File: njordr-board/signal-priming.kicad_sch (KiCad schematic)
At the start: 42 parts, among them IC2 GS8054, IC3 TMUX741x, T1 TestPoint, T10 TestPoint, T11 TestPoint, T2 TestPoint, T9 TestPoint, U3 REF3012, U7 LM393

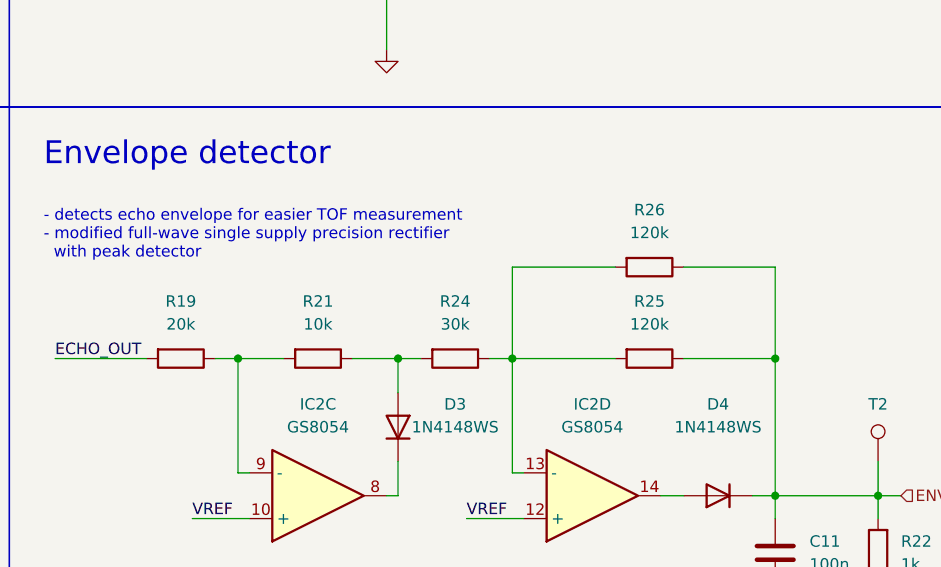
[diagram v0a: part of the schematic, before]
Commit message: board: Use lower resistor values for the envelope detector
- try to lower impedance to have higher stability
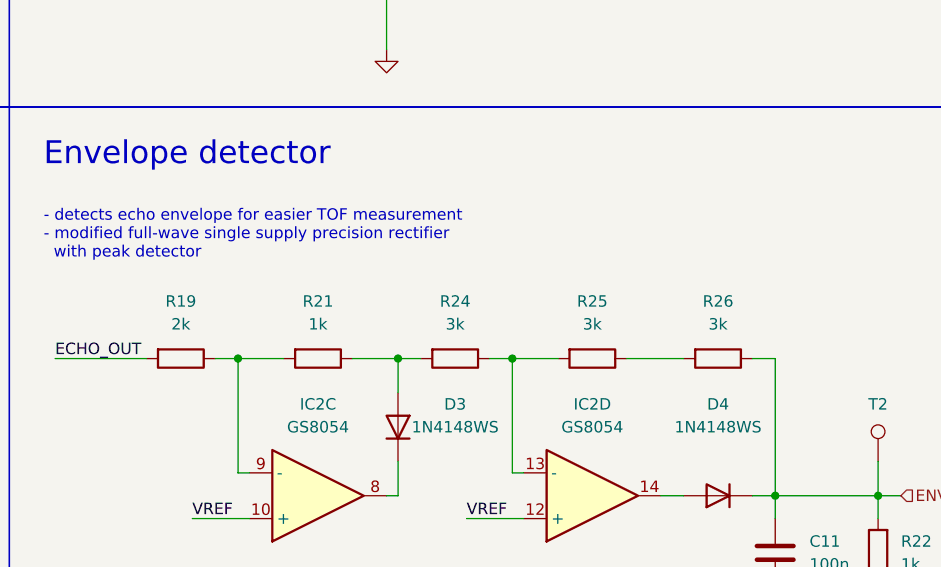
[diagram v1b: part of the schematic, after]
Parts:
- R19: value 20k -> 2k; LCSC (none) -> C22975
- R21: value 10k -> 1k; LCSC C15401 -> C21190
- R22: LCSC (none) -> C21190
- R24: value 30k -> 3k; LCSC (none) -> C4211
- R25, R26: value 120k -> 3k; LCSC (none) -> C4211
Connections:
- net ENVELOPE: no longer R25.1
- net at IC2.13 (-), R24.1, R25.2: no longer R26.2
- new net: R25.1, R26.2
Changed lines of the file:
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@@
 	)
 	(junction
-		(at 254 120.65)
-		(diameter 0)
-		(color 0 0 0 0)
-	)
-	(junction
 		(at 265.43 135.89)
 		(diameter 0)
@@
 	(wire
 		(pts
-			(xy 224.79 110.49) (xy 236.22 110.49)
-		)
-		(stroke
-			(width 0)
-			(type default)
-		)
-	)
-	(wire
-		(pts
 			(xy 55.88 135.89) (xy 55.88 143.51)
 		)
@@
 	(wire
 		(pts
-			(xy 224.79 120.65) (xy 224.79 110.49)
+			(xy 39.37 170.18) (xy 39.37 172.72)
 		)
 		(stroke
@@
 	(wire
 		(pts
-			(xy 39.37 170.18) (xy 39.37 172.72)
+			(xy 66.04 135.89) (xy 66.04 143.51)
 		)
 		(stroke
@@
 	(wire
 		(pts
-			(xy 66.04 135.89) (xy 66.04 143.51)
+			(xy 237.49 120.65) (xy 243.84 120.65)
 		)
 		(stroke
@@
 	(wire
 		(pts
-			(xy 224.79 120.65) (xy 236.22 120.65)
+			(xy 224.79 120.65) (xy 229.87 120.65)
 		)
 		(stroke
@@
 	(wire
 		(pts
-			(xy 254 110.49) (xy 254 120.65)
-		)
-		(stroke
-			(width 0)
-			(type default)
-		)
-	)
-	(wire
-		(pts
 			(xy 212.09 132.08) (xy 212.09 135.89)
 		)
@@
 	(wire
 		(pts
-			(xy 243.84 110.49) (xy 254 110.49)
+			(xy 251.46 120.65) (xy 254 120.65)
 		)
 		(stroke
@@
 		)
 	)
-	(wire
-		(pts
-			(xy 243.84 120.65) (xy 254 120.65)
-		)
-		(stroke
-			(width 0)
-			(type default)
-		)
-	)
 	(label "ECHO_IN"
 		(at 102.87 233.68 180)
@@
 	(symbol
 		(lib_id "Device:R")
+		(at 233.68 120.65 270)
+		(unit 1)
+		(exclude_from_sim no)
+		(in_bom yes)
+		(on_board yes)
+		(dnp no)
+		(fields_autoplaced yes)
+		(property "Reference" "R25"
+			(at 233.68 114.3 90)
+			(effects
+				(font
+					(size 1.27 1.27)
+				)
+			)
+		)
+		(property "Value" "3k"
+			(at 233.68 116.84 90)
+			(effects
+				(font
+					(size 1.27 1.27)
+				)
+			)
+		)
+		(property "Footprint" "njordr:R_0603_1608Metric_Pad0.98x0.95mm_HandSolder"
+			(at 233.68 118.872 90)
+			(effects
+				(font
+					(size 1.27 1.27)
+				)
+				(hide yes)
+			)
+		)
+		(property "Datasheet" "https://jlcpcb.com/partdetail/21904-0603WAF1001T5E/C21190"
+			(at 233.68 120.65 0)
+			(effects
+				(font
+					(size 1.27 1.27)
+				)
+				(hide yes)
+			)
+		)
+		(property "Description" "Resistor"
+			(at 233.68 120.65 0)
+			(effects
+				(font
+					(size 1.27 1.27)
+				)
+				(hide yes)
+			)
+		)
+		(property "LCSC" "C4211"
+			(at 233.68 120.65 90)
+			(effects
+				(font
+					(size 1.27 1.27)
+				)
+				(hide yes)
+			)
+		)
+		(pin "1"
+		)
+		(pin "2"
+		)
+		(instances
+			(project "njordr-board"
+				(path "/837a3018-1957-4824-b018-c0ef83e9cb67/55a1aa29-8230-4b58-97dd-4caaf3e17561"
+					(reference "R25")
+					(unit 1)
+				)
+			)
+		)
+	)
+	(symbol
+		(lib_id "Device:R")
 		(at 223.52 50.8 180)
 		(unit 1)
@@
 	)
 	(symbol
-		(lib_id "Device:R")
-		(at 240.03 110.49 270)
-		(unit 1)
-		(exclude_from_sim no)
-		(in_bom yes)
-		(on_board yes)
-		(dnp no)
-		(fields_autoplaced yes)
-		(property "Reference" "R26"
-			(at 240.03 104.14 90)
-			(effects
-				(font
-					(size 1.27 1.27)
-				)
-			)
-		)
-		(property "Value" "120k"
-			(at 240.03 106.68 90)
-			(effects
-				(font
-					(size 1.27 1.27)
-				)
-			)
-		)
-		(property "Footprint" "njordr:R_0603_1608Metric_Pad0.98x0.95mm_HandSolder"
-			(at 240.03 108.712 90)
-			(effects
-				(font
-					(size 1.27 1.27)
-				)
-				(hide yes)
-			)
-		)
-		(property "Datasheet" "https://jlcpcb.com/partdetail/21904-0603WAF1001T5E/C21190"
-			(at 240.03 110.49 0)
-			(effects
-				(font
-					(size 1.27 1.27)
-				)
-				(hide yes)
-			)
-		)
-		(property "Description" "Resistor"
-			(at 240.03 110.49 0)
-			(effects
-				(font
-					(size 1.27 1.27)
-				)
-				(hide yes)
-			)
-		)
-		(property "LCSC" ""
-			(at 240.03 110.49 90)
-			(effects
-				(font
-					(size 1.27 1.27)
-				)
-				(hide yes)
-			)
-		)
-		(pin "1"
-		)
-		(pin "2"
-		)
-		(instances
-			(project "njordr-board"
-				(path "/837a3018-1957-4824-b018-c0ef83e9cb67/55a1aa29-8230-4b58-97dd-4caaf3e17561"
-					(reference "R26")
-					(unit 1)
-				)
-			)
-		)
-	)
-	(symbol
 		(lib_id "power:+24V")
 		(at 55.88 41.91 0)
@@
 			)
 		)
-		(property "Value" "10k"
+		(property "Value" "1k"
 			(at 203.2 116.84 90)
 			(effects
@@
 			)
 		)
-		(property "LCSC" "C15401"
+		(property "LCSC" "C21190"
 			(at 203.2 120.65 0)
 			(effects
@@
 			)
 		)
-		(property "Value" "30k"
+		(property "Value" "3k"
 			(at 218.44 116.84 90)
 			(effects
@@
 			)
 		)
-		(property "LCSC" ""
+		(property "LCSC" "C4211"
 			(at 218.44 120.65 90)
 			(effects
@@
 	)
 	(symbol
+		(lib_id "Device:R")
+		(at 247.65 120.65 270)
+		(unit 1)
+		(exclude_from_sim no)
+		(in_bom yes)
+		(on_board yes)
+		(dnp no)
+		(fields_autoplaced yes)
+		(property "Reference" "R26"
+			(at 247.65 114.3 90)
+			(effects
+				(font
+					(size 1.27 1.27)
+				)
+			)
+		)
+		(property "Value" "3k"
+			(at 247.65 116.84 90)
+			(effects
+				(font
+					(size 1.27 1.27)
+				)
+			)
+		)
+		(property "Footprint" "njordr:R_0603_1608Metric_Pad0.98x0.95mm_HandSolder"
+			(at 247.65 118.872 90)
+			(effects
+				(font
+					(size 1.27 1.27)
+				)
+				(hide yes)
+			)
+		)
+		(property "Datasheet" "https://jlcpcb.com/partdetail/21904-0603WAF1001T5E/C21190"
+			(at 247.65 120.65 0)
+			(effects
+				(font
+					(size 1.27 1.27)
+				)
+				(hide yes)
+			)
+		)
+		(property "Description" "Resistor"
+			(at 247.65 120.65 0)
+			(effects
+				(font
+					(size 1.27 1.27)
+				)
+				(hide yes)
+			)
+		)
+		(property "LCSC" "C4211"
+			(at 247.65 120.65 90)
+			(effects
+				(font
+					(size 1.27 1.27)
+				)
+				(hide yes)
+			)
+		)
+		(pin "1"
+		)
+		(pin "2"
+		)
+		(instances
+			(project "njordr-board"
+				(path "/837a3018-1957-4824-b018-c0ef83e9cb67/55a1aa29-8230-4b58-97dd-4caaf3e17561"
+					(reference "R26")
+					(unit 1)
+				)
+			)
+		)
+	)
+	(symbol
 		(lib_id "TL974IPWR:TL974IPWR")
 		(at 68.58 184.15 0)
@@
 			)
 		)
-		(property "LCSC" ""
+		(property "LCSC" "C21190"
 			(at 265.43 142.24 90)
 			(effects
@@
 			)
 		)
-		(property "Value" "20k"
+		(property "Value" "2k"
 			(at 187.96 116.84 90)
 			(effects
@@
 			)
 		)
-		(property "LCSC" ""
+		(property "LCSC" "C22975"
 			(at 187.96 120.65 90)
 			(effects
@@
 					(unit 1)
 				)
-			)
-		)
-	)
-	(symbol
-		(lib_id "Device:R")
-		(at 240.03 120.65 270)
-		(unit 1)
-		(exclude_from_sim no)
-		(in_bom yes)
-		(on_board yes)
-		(dnp no)
-		(fields_autoplaced yes)
-		(property "Reference" "R25"
-			(at 240.03 114.3 90)
-			(effects
-				(font
-					(size 1.27 1.27)
-				)
-			)
-		)
-		(property "Value" "120k"
-			(at 240.03 116.84 90)
-			(effects
-				(font
-					(size 1.27 1.27)
-				)
-			)
-		)
-		(property "Footprint" "njordr:R_0603_1608Metric_Pad0.98x0.95mm_HandSolder"
-			(at 240.03 118.872 90)
-			(effects
-				(font
-					(size 1.27 1.27)
-				)
-				(hide yes)
-			)
-		)
-		(property "Datasheet" "https://jlcpcb.com/partdetail/21904-0603WAF1001T5E/C21190"
-			(at 240.03 120.65 0)
-			(effects
-				(font
-					(size 1.27 1.27)
-				)
-				(hide yes)
-			)
-		)
-		(property "Description" "Resistor"
-			(at 240.03 120.65 0)
-			(effects
-				(font
-					(size 1.27 1.27)
-				)
-				(hide yes)
-			)
-		)
-		(property "LCSC" ""
-			(at 240.03 120.65 90)
-			(effects
-				(font
-					(size 1.27 1.27)
-				)
-				(hide yes)
-			)
-		)
-		(pin "1"
-		)
-		(pin "2"
-		)
-		(instances
-			(project "njordr-board"
-				(path "/837a3018-1957-4824-b018-c0ef83e9cb67/55a1aa29-8230-4b58-97dd-4caaf3e17561"
-					(reference "R25")
-					(unit 1)
-				)

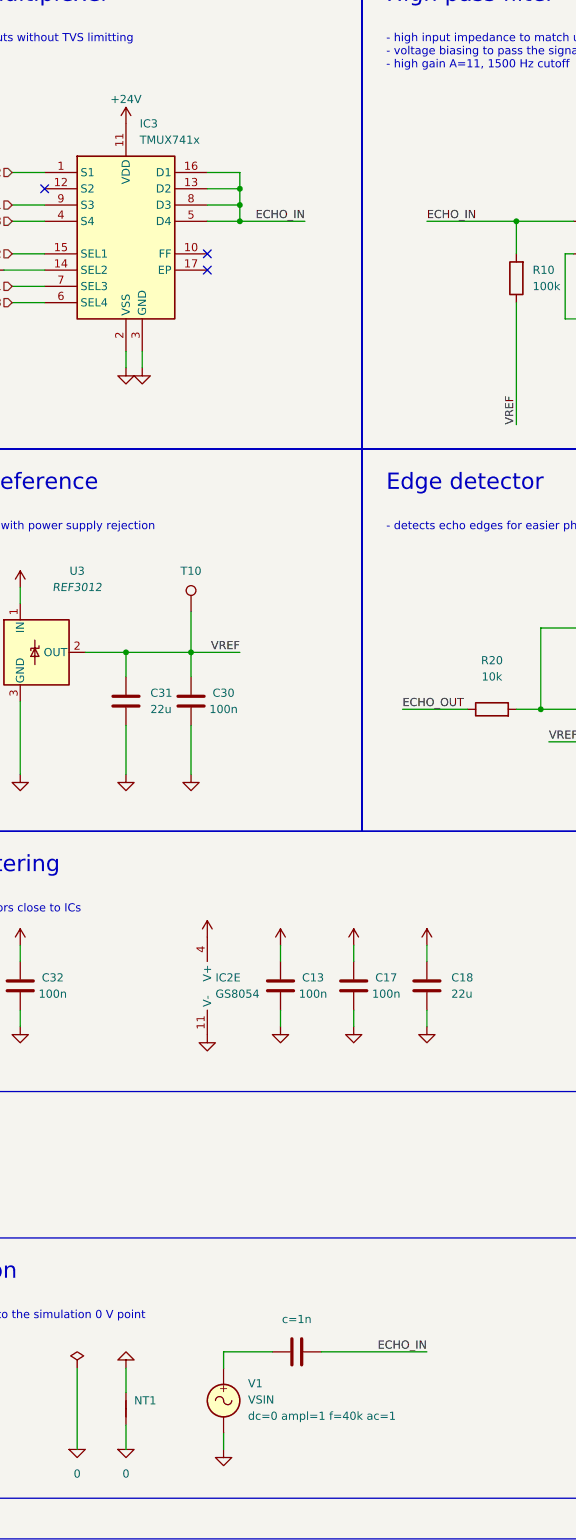
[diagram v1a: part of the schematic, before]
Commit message: njordr-board: Use updated library symbols and packages
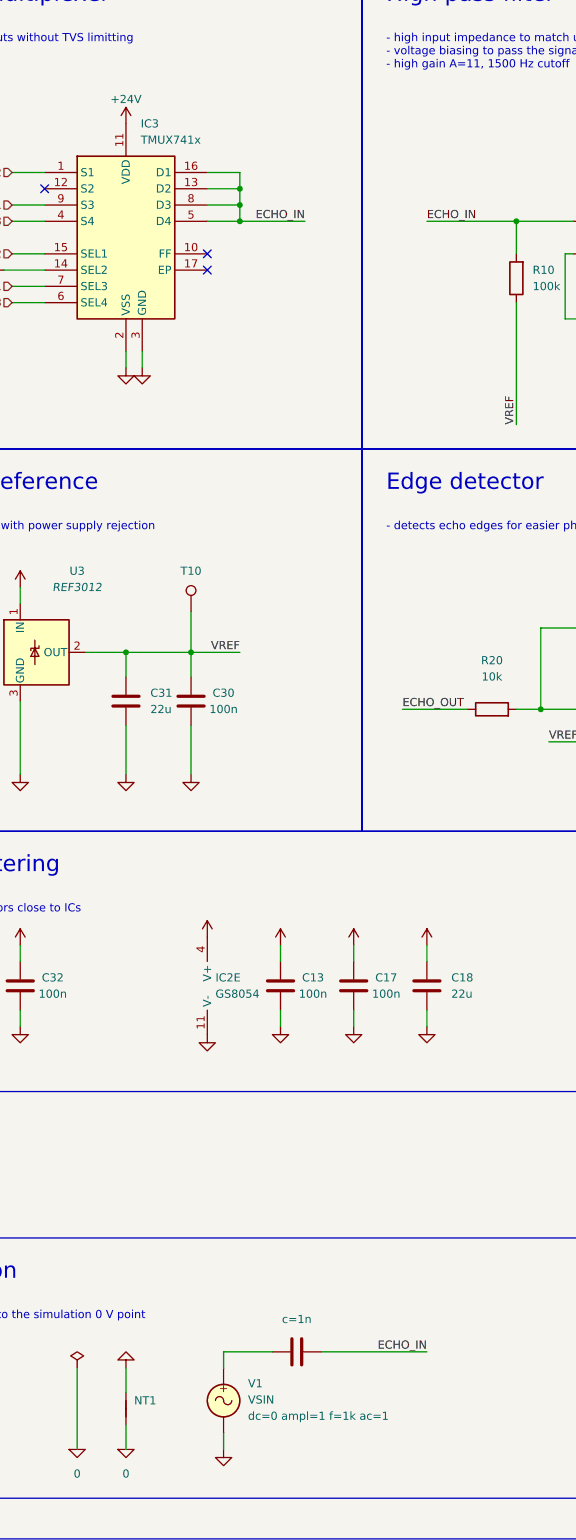
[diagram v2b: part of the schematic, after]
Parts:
- C11, C13, C17, C20, C30, C32, C6, C7, C9: footprint njordr:C_0603_1608Metric_Pad1.08x0.95mm_HandSolder -> njordr:C-0603-HandSolder
- C18, C21, C31: footprint njordr:C_0805_2012Metric_Pad1.18x1.45mm_HandSolder -> njordr:C-0805-HandSolder
- D3, D4: footprint njordr:D_SOD-323_HandSoldering -> njordr:D-SOD-323-HandSolder
- IC2: symbol TL974IPWR:TL974IPWR -> njordr:TL974IPWR; LCSC C431327 -> C128406
- IC3: symbol TMUX7411FRRPR:TMUX741x -> njordr:TMUX741x
- R10, R11, R12, R13, R14, R15, R16, R19, R20, R21, R22, R23, R24, R25, R26: footprint njordr:R_0603_1608Metric_Pad0.98x0.95mm_HandSolder -> njordr:R-0603-HandSolder
- T1, T10, T11, T2, T9: footprint njordr:TestPoint_Pad_1.0x1.0mm -> njordr:TestPoint-Pad-1.0x1.0
- U7: footprint njordr:SOIC-8_3.9x4.9mm_P1.27mm -> njordr:SOIC-8-3.9x4.9-P1.27
